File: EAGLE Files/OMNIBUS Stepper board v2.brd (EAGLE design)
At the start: 100.6 x 73.6 mm, 52 parts, among them IC1 REG1117, K7 691131710005, K8 691131710005, K9 691131710005, Q1 BTS134D, U2 L7805ACD2T-TR

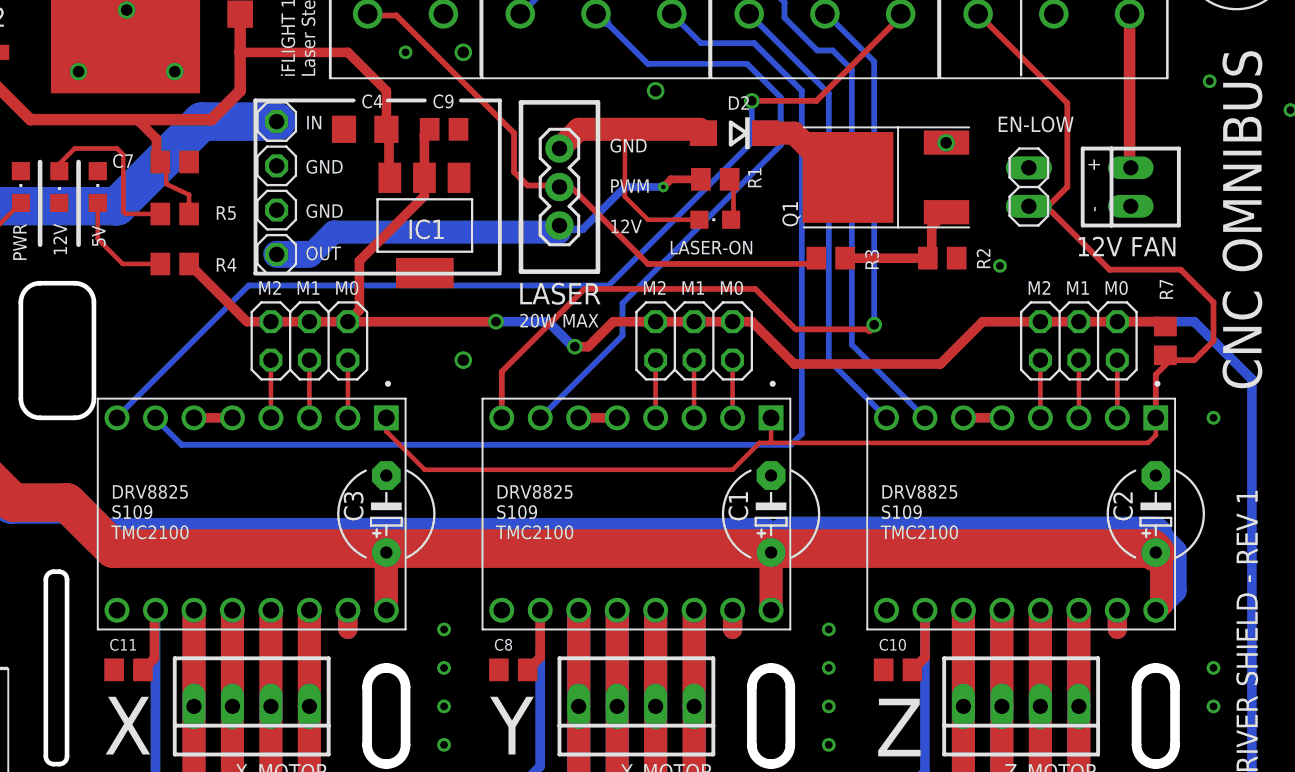
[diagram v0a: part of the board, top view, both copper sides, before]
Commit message: PCB Bugfixes and polishing
• DRV Shield had an routing error (laser indicator LED) also R3 had a wrong value
• New Footprint for the 0.33uF Caps
• Silkscreen polishing
• almost all LEDs are 0805 package now
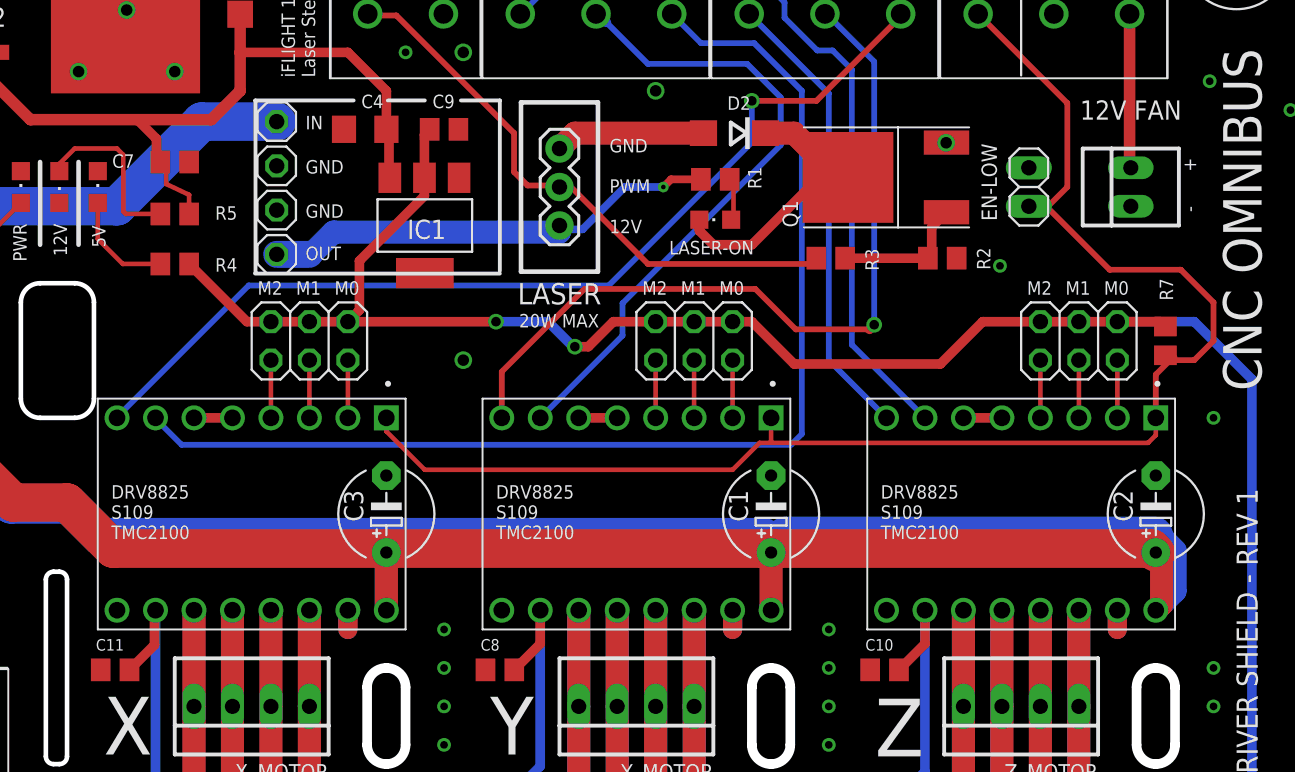
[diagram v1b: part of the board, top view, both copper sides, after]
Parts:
- R3: value 10k -> 470
- moved C11 0.89 mm to (18.9, 20.2)
- moved C8 0.89 mm to (44.3, 20.2)
- moved C10 0.89 mm to (69.7, 20.2)
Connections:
- net L_SW: now also D2.C, Q1.T; no longer D2.A, J1.3
- net N$4: now also D2.A, J1.3; no longer D2.C, Q1.T
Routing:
- net N$4: track 8.10 -> 9.93 mm
- net 5V: track 286.8 -> 287.9 mm
- net L_SW: track 20.1 -> 19.3 mm
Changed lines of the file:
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@@
 <drawing>
 <settings>
-<setting alwaysvectorfont="no"/>
+<setting alwaysvectorfont="yes"/>
 <setting verticaltext="up"/>
 </settings>
@@
 <text x="80.645" y="71.501" size="0.889" layer="25" font="vector" ratio="15" rot="SR180" align="bottom-center">GND</text>
 <text x="85.217" y="71.501" size="0.889" layer="25" font="vector" ratio="15" rot="SR180" align="bottom-center">12V-OUT</text>
-<text x="85.725" y="47.498" size="1.27" layer="25" font="vector" ratio="15" align="bottom-center">12V FAN</text>
+<text x="85.979" y="56.515" size="1.27" layer="25" font="vector" ratio="15" align="bottom-center">12V FAN</text>
 <text x="94.615" y="49.911" size="2.54" layer="25" font="vector" ratio="20" rot="SR90" align="bottom-center">CNC OMNIBUS</text>
 <text x="94.361" y="22.098" size="1.397" layer="25" font="vector" ratio="15" rot="SR90" align="bottom-center">DRIVER SHIELD - REV 1</text>
@@
 <wire x1="13.97" y1="53.721" x2="13.97" y2="48.26" width="0.3048" layer="25"/>
 <wire x1="16.51" y1="53.721" x2="16.51" y2="48.26" width="0.3048" layer="25"/>
-<text x="83.947" y="53.086" size="0.889" layer="25" font="vector" ratio="15" rot="R90">+</text>
+<text x="90.297" y="53.086" size="0.889" layer="25" font="vector" ratio="15" rot="R90">+</text>
 <text x="29.972" y="45.847" size="0.889" layer="25" font="vector" ratio="15" rot="R180">M2</text>
 <text x="32.512" y="45.847" size="0.889" layer="25" font="vector" ratio="15" rot="R180">M1</text>
@@
 TMC2100</text>
 <text x="-0.508" y="37.338" size="0.889" layer="25" font="vector" ratio="15" rot="SR270">MAX CURRENT: 10A</text>
-<text x="83.947" y="50.419" size="0.889" layer="25" font="vector" ratio="15" rot="R90">-</text>
+<text x="90.297" y="50.419" size="0.889" layer="25" font="vector" ratio="15" rot="R90">-</text>
 <text x="44.069" y="28.829" size="0.889" layer="25" font="vector" ratio="15">DRV8825
 S109
@@
 </element>
 <element name="EN-LOW" library="pinhead" library_urn="urn:adsk.eagle:library:325" package="1X02" package3d_urn="urn:adsk.eagle:package:22435/2" value="" x="79.248" y="52.07" smashed="yes" rot="R270">
-<attribute name="NAME" x="82.2452" y="56.7182" size="1.016" layer="25" font="vector" ratio="10" rot="R180"/>
+<attribute name="NAME" x="76.1238" y="54.9402" size="1.016" layer="25" font="vector" ratio="20" rot="R270"/>
 <attribute name="POPULARITY" value="98" x="79.248" y="52.07" size="1.778" layer="27" rot="R270" display="off"/>
 <attribute name="VALUE" x="76.073" y="54.61" size="1.27" layer="27" rot="R270"/>
@@
 <attribute name="VALUE" x="63.319" y="1.592" size="1.27" layer="27"/>
 </element>
-<element name="R3" library="rcl" library_urn="urn:adsk.eagle:library:334" package="R0805" package3d_urn="urn:adsk.eagle:package:23553/2" value="10k" x="66.167" y="47.371" smashed="yes" rot="R180">
+<element name="R3" library="rcl" library_urn="urn:adsk.eagle:library:334" package="R0805" package3d_urn="urn:adsk.eagle:package:23553/2" value="470" x="66.167" y="47.371" smashed="yes" rot="R180">
 <attribute name="NAME" x="68.453" y="48.006" size="0.889" layer="25" font="vector" ratio="10" rot="R270"/>
 <attribute name="POPULARITY" value="86" x="66.167" y="47.371" size="1.778" layer="27" rot="R180" display="off"/>
@@
 <attribute name="VALUE" x="28.321" y="44.45" size="1.27" layer="27"/>
 </element>
-<element name="C8" library="rcl" library_urn="urn:adsk.eagle:library:334" package="C0805" package3d_urn="urn:adsk.eagle:package:23617/2" value="100nf" x="45.212" y="20.193" smashed="yes">
-<attribute name="NAME" x="43.942" y="21.463" size="0.762" layer="25" font="vector" ratio="10"/>
-<attribute name="SPICEPREFIX" value="C" x="45.212" y="20.193" size="1.778" layer="27" display="off"/>
-<attribute name="VALUE" x="43.942" y="17.653" size="1.27" layer="27"/>
-</element>
-<element name="C10" library="rcl" library_urn="urn:adsk.eagle:library:334" package="C0805" package3d_urn="urn:adsk.eagle:package:23617/2" value="100nf" x="70.612" y="20.193" smashed="yes">
-<attribute name="NAME" x="69.342" y="21.463" size="0.762" layer="25" font="vector" ratio="10"/>
-<attribute name="SPICEPREFIX" value="C" x="70.612" y="20.193" size="1.778" layer="27" display="off"/>
-<attribute name="VALUE" x="69.342" y="17.653" size="1.27" layer="27"/>
-</element>
-<element name="C11" library="rcl" library_urn="urn:adsk.eagle:library:334" package="C0805" package3d_urn="urn:adsk.eagle:package:23617/2" value="100nf" x="19.812" y="20.193" smashed="yes">
-<attribute name="NAME" x="18.542" y="21.463" size="0.762" layer="25" font="vector" ratio="10"/>
-<attribute name="SPICEPREFIX" value="C" x="19.812" y="20.193" size="1.778" layer="27" display="off"/>
-<attribute name="VALUE" x="18.542" y="17.653" size="1.27" layer="27"/>
+<element name="C8" library="rcl" library_urn="urn:adsk.eagle:library:334" package="C0805" package3d_urn="urn:adsk.eagle:package:23617/2" value="100nf" x="44.323" y="20.193" smashed="yes">
+<attribute name="NAME" x="43.053" y="21.463" size="0.762" layer="25" font="vector" ratio="10"/>
+<attribute name="SPICEPREFIX" value="C" x="44.323" y="20.193" size="1.778" layer="27" display="off"/>
+<attribute name="VALUE" x="43.053" y="17.653" size="1.27" layer="27"/>
+</element>
+<element name="C10" library="rcl" library_urn="urn:adsk.eagle:library:334" package="C0805" package3d_urn="urn:adsk.eagle:package:23617/2" value="100nf" x="69.723" y="20.193" smashed="yes">
+<attribute name="NAME" x="68.453" y="21.463" size="0.762" layer="25" font="vector" ratio="10"/>
+<attribute name="SPICEPREFIX" value="C" x="69.723" y="20.193" size="1.778" layer="27" display="off"/>
+<attribute name="VALUE" x="68.453" y="17.653" size="1.27" layer="27"/>
+</element>
+<element name="C11" library="rcl" library_urn="urn:adsk.eagle:library:334" package="C0805" package3d_urn="urn:adsk.eagle:package:23617/2" value="100nf" x="18.923" y="20.193" smashed="yes">
+<attribute name="NAME" x="17.653" y="21.463" size="0.762" layer="25" font="vector" ratio="10"/>
+<attribute name="SPICEPREFIX" value="C" x="18.923" y="20.193" size="1.778" layer="27" display="off"/>
+<attribute name="VALUE" x="17.653" y="17.653" size="1.27" layer="27"/>
 </element>
 </elements>
@@
 <contactref element="C11" pad="2"/>
 <contactref element="C8" pad="2"/>
-<wire x1="21.524" y1="24.064" x2="21.524" y2="20.955" width="0.635" layer="1"/>
-<wire x1="20.762" y1="20.193" x2="21.524" y2="20.955" width="0.635" layer="1"/>
+<wire x1="21.524" y1="24.064" x2="21.524" y2="21.844" width="0.635" layer="1"/>
+<wire x1="19.873" y1="20.193" x2="21.524" y2="21.844" width="0.635" layer="1"/>
 <wire x1="21.524" y1="24.064" x2="21.59" y2="24.13" width="0.635" layer="1"/>
-<wire x1="46.162" y1="20.193" x2="46.99" y2="21.021" width="0.635" layer="1"/>
-<wire x1="46.99" y1="21.021" x2="46.99" y2="24.13" width="0.635" layer="1"/>
-<wire x1="71.562" y1="20.193" x2="72.39" y2="21.021" width="0.635" layer="1"/>
-<wire x1="72.39" y1="21.021" x2="72.39" y2="24.13" width="0.635" layer="1"/>
+<wire x1="45.273" y1="20.193" x2="46.99" y2="21.91" width="0.635" layer="1"/>
+<wire x1="46.99" y1="21.91" x2="46.99" y2="24.13" width="0.635" layer="1"/>
+<wire x1="70.673" y1="20.193" x2="72.39" y2="21.91" width="0.635" layer="1"/>
+<wire x1="72.39" y1="21.91" x2="72.39" y2="24.13" width="0.635" layer="1"/>
 </signal>
 <signal name="X_DIR" class="1">
@@
 </signal>
 <signal name="L_SW" class="1">
-<contactref element="D2" pad="A"/>
 <contactref element="LASER-ON" pad="C"/>
-<wire x1="52.578" y1="55.88" x2="57.513" y2="55.88" width="1.524" layer="1"/>
-<wire x1="57.513" y1="55.88" x2="57.767" y2="55.626" width="1.524" layer="1"/>
-<wire x1="57.497" y1="49.911" x2="54.102" y2="49.911" width="0.3048" layer="1"/>
-<wire x1="54.102" y1="49.911" x2="52.578" y2="51.435" width="0.3048" layer="1"/>
-<wire x1="52.578" y1="51.435" x2="52.578" y2="55.88" width="0.3048" layer="1"/>
-<contactref element="J1" pad="3"/>
-<wire x1="52.578" y1="55.88" x2="49.53" y2="55.88" width="1.524" layer="1"/>
-<wire x1="49.53" y1="55.88" x2="48.26" y2="54.61" width="1.524" layer="1"/>
+<contactref element="D2" pad="C"/>
+<contactref element="Q1" pad="T"/>
+<wire x1="61.867" y1="55.626" x2="63.754" y2="55.626" width="1.524" layer="1"/>
+<wire x1="63.754" y1="55.626" x2="66.04" y2="53.34" width="1.524" layer="1"/>
+<wire x1="66.04" y1="51.943" x2="66.04" y2="53.34" width="1.524" layer="1"/>
+<wire x1="67.31" y1="52.705" x2="66.548" y2="51.943" width="0.635" layer="1"/>
+<wire x1="66.548" y1="51.943" x2="66.04" y2="51.943" width="0.635" layer="1"/>
+<wire x1="57.497" y1="49.911" x2="57.497" y2="49.183" width="0.635" layer="1"/>
+<wire x1="57.497" y1="49.183" x2="58.42" y2="48.26" width="0.635" layer="1"/>
+<wire x1="58.42" y1="48.26" x2="60.96" y2="48.26" width="0.635" layer="1"/>
+<wire x1="64.643" y1="51.943" x2="66.04" y2="51.943" width="0.635" layer="1"/>
+<wire x1="60.96" y1="48.26" x2="64.643" y2="51.943" width="0.635" layer="1"/>
 </signal>
 <signal name="5VPWM" class="1">
@@
 <contactref element="JP1" pad="1"/>
 </signal>
-<signal name="N$4" class="1">
-<contactref element="D2" pad="C"/>
-<wire x1="61.867" y1="55.626" x2="63.754" y2="55.626" width="1.524" layer="1"/>
-<wire x1="63.754" y1="55.626" x2="66.04" y2="53.34" width="1.524" layer="1"/>
-<wire x1="66.04" y1="51.943" x2="66.04" y2="53.34" width="1.524" layer="1"/>
-<contactref element="Q1" pad="T"/>
-<wire x1="67.31" y1="52.705" x2="66.548" y2="51.943" width="0.635" layer="1"/>
-<wire x1="66.548" y1="51.943" x2="66.04" y2="51.943" width="0.635" layer="1"/>
-</signal>
 <signal name="N$2">
 <contactref element="R4" pad="2"/>
@@
 <wire x1="26.67" y1="36.83" x2="24.13" y2="36.83" width="0.635" layer="1"/>
 </signal>
+<signal name="N$4" class="1">
+<contactref element="D2" pad="A"/>
+<contactref element="J1" pad="3"/>
+<wire x1="48.26" y1="54.61" x2="49.276" y2="55.626" width="1.524" layer="1"/>
+<wire x1="49.276" y1="55.626" x2="57.767" y2="55.626" width="1.524" layer="1"/>
+</signal>
 </signals>

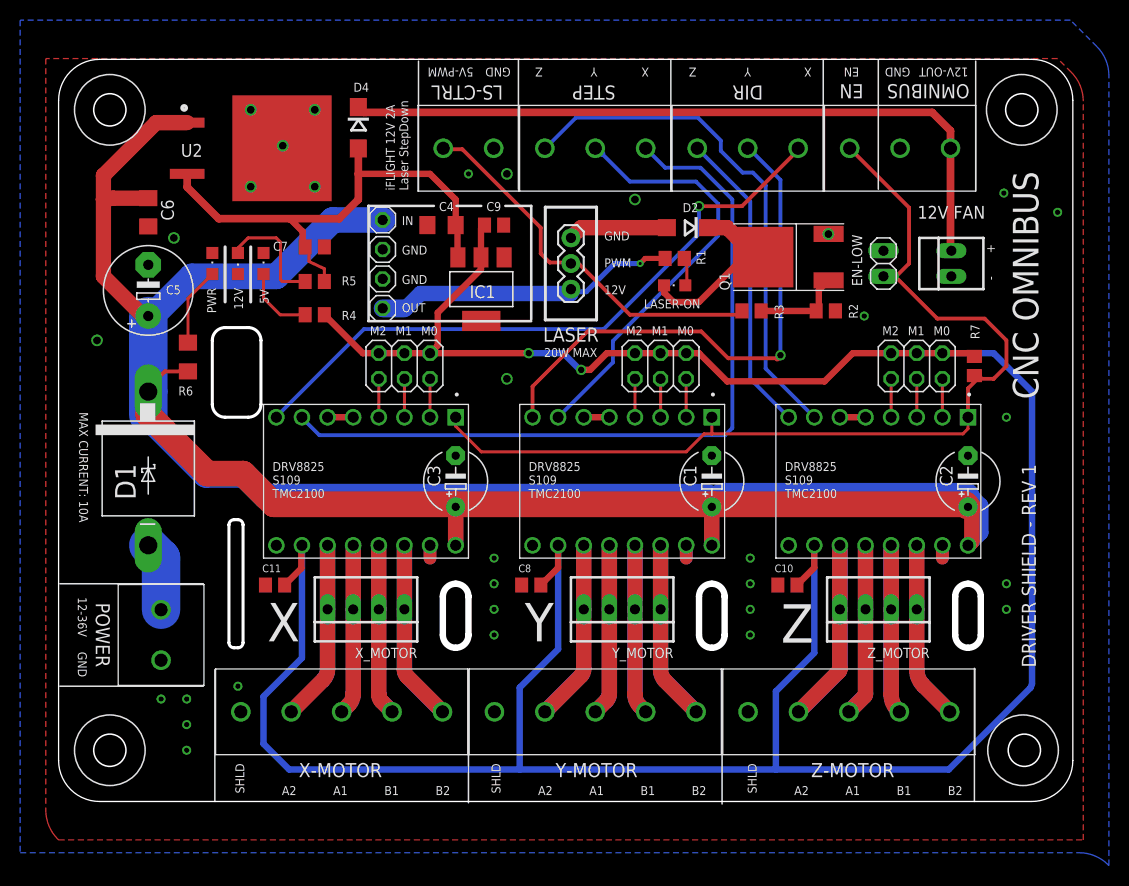
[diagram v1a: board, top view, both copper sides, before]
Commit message: Changed voltage regulators
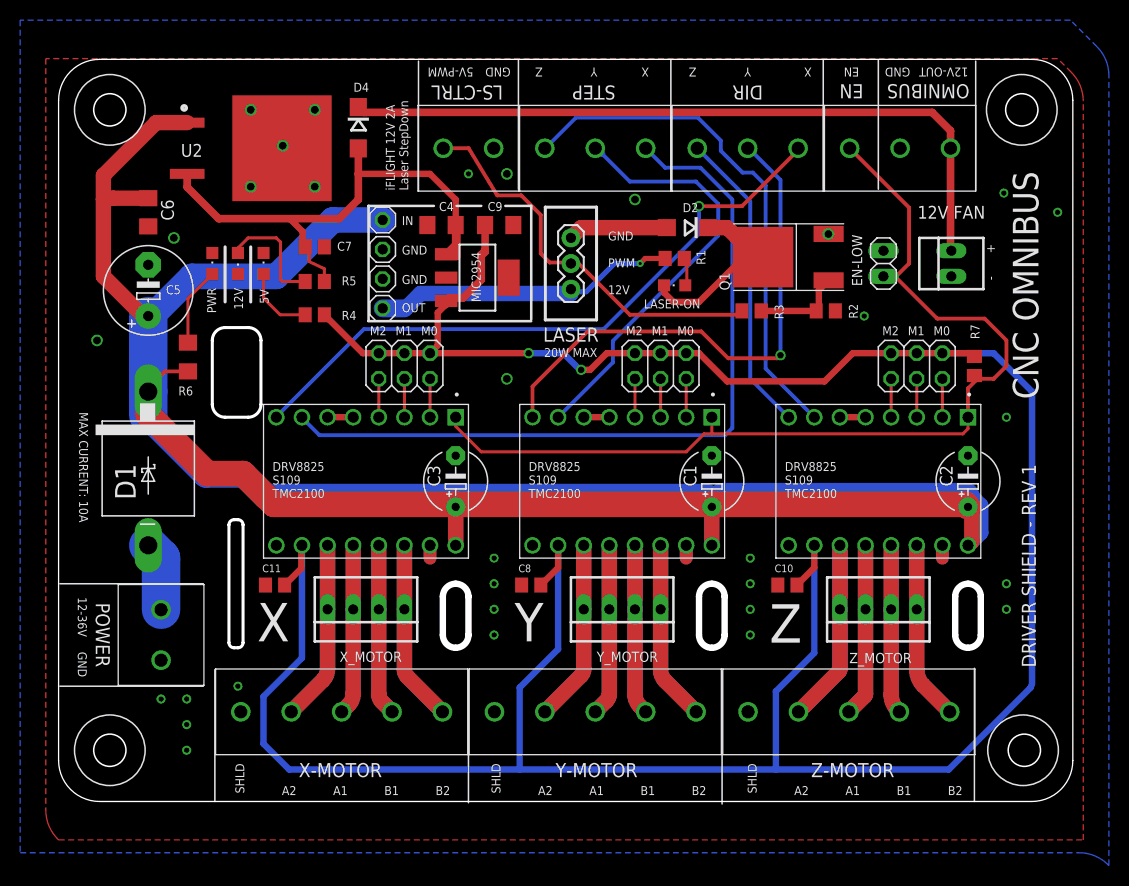
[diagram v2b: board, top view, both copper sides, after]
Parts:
- removed IC1: REG1117, burr-brown:SOT223
- added MIC2954: MIC2954, MIC2954:SOT223
- C9: device rcl:C0805 -> rcl:C1206
- moved C9 0.51 mm to (41.1, 55.9)
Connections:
- net N$4 renamed GND_SW
- net 12V_BD: now also MIC2954.1; no longer IC1.3
- net 5V: now also MIC2954.3; no longer IC1.2
- net GND: now also MIC2954.2, MIC2954.4; no longer IC1.1
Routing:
- net 12V_BD: track 50.0 -> 53.2 mm
- net 5VPWM: track 38.2 -> 39.6 mm
- net 5V: track 287.9 -> 289.1 mm

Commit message: clean up
also added BOM
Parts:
- 12V, 5V, PWR: value (none) -> green
- renumbered RAW1 to PWM
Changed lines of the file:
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@@
 <drawing>
 <settings>
-<setting alwaysvectorfont="yes"/>
+<setting alwaysvectorfont="no"/>
 <setting verticaltext="up"/>
 </settings>
@@
 <attribute name="VALUE" x="9.3726" y="46.8884" size="1.27" layer="27" ratio="10" rot="R90"/>
 </element>
-<element name="RAW1" library="Wurth_Terminal_Blocks_Connectors_rev15d" package="691131710002" value="691131710002" x="38.1" y="63.5" smashed="yes" rot="R180">
+<element name="PWM" library="Wurth_Terminal_Blocks_Connectors_rev15d" package="691131710002" value="691131710002" x="38.1" y="63.5" smashed="yes" rot="R180">
 <attribute name="VALUE" x="43.1" y="69.528" size="1.27" layer="27" rot="R180"/>
 </element>
@@
 <attribute name="VALUE" x="23.495" y="49.53" size="1.27" layer="27" rot="R180"/>
 </element>
-<element name="5V" library="led" library_urn="urn:adsk.eagle:library:259" package="CHIPLED_0805" package3d_urn="urn:adsk.eagle:package:15821/2" value="" x="17.78" y="52.07" smashed="yes">
+<element name="5V" library="led" library_urn="urn:adsk.eagle:library:259" package="CHIPLED_0805" package3d_urn="urn:adsk.eagle:package:15821/2" value="green" x="17.78" y="52.07" smashed="yes">
 <attribute name="NAME" x="17.399" y="49.53" size="0.889" layer="25" font="vector" ratio="10" rot="R270"/>
 <attribute name="VALUE" x="20.32" y="50.8" size="1.27" layer="27" rot="R90"/>
@@
 <attribute name="VALUE" x="23.495" y="52.832" size="1.27" layer="27" rot="R180"/>
 </element>
-<element name="12V" library="led" library_urn="urn:adsk.eagle:library:259" package="CHIPLED_0805" package3d_urn="urn:adsk.eagle:package:15821/2" value="" x="15.24" y="52.07" smashed="yes" rot="R180">
+<element name="12V" library="led" library_urn="urn:adsk.eagle:library:259" package="CHIPLED_0805" package3d_urn="urn:adsk.eagle:package:15821/2" value="green" x="15.24" y="52.07" smashed="yes" rot="R180">
 <attribute name="NAME" x="14.859" y="49.657" size="0.889" layer="25" font="vector" ratio="10" rot="R270"/>
 <attribute name="VALUE" x="12.7" y="53.34" size="1.27" layer="27" rot="R270"/>
@@
 <attribute name="VALUE" x="12.827" y="42.164" size="1.27" layer="27" rot="R90"/>
 </element>
-<element name="PWR" library="led" library_urn="urn:adsk.eagle:library:259" package="CHIPLED_0805" package3d_urn="urn:adsk.eagle:package:15821/2" value="" x="12.7" y="52.07" smashed="yes">
+<element name="PWR" library="led" library_urn="urn:adsk.eagle:library:259" package="CHIPLED_0805" package3d_urn="urn:adsk.eagle:package:15821/2" value="green" x="12.7" y="52.07" smashed="yes">
 <attribute name="NAME" x="12.192" y="49.657" size="0.889" layer="25" font="vector" ratio="10" rot="R270"/>
 <attribute name="VALUE" x="15.24" y="50.8" size="1.27" layer="27" rot="R90"/>
@@
 <contactref element="K7" pad="1"/>
 <contactref element="R2" pad="2"/>
-<contactref element="RAW1" pad="1"/>
+<contactref element="PWM" pad="1"/>
 <contactref element="C5" pad="-"/>
 <contactref element="12V" pad="C"/>
@@
 <signal name="5VPWM" class="1">
 <contactref element="R3" pad="2"/>
-<contactref element="RAW1" pad="2"/>
+<contactref element="PWM" pad="2"/>
 <wire x1="35.6" y1="63.5" x2="35.56" y2="63.5" width="0.3048" layer="16"/>
 <wire x1="64.836" y1="46.99" x2="65.217" y2="47.371" width="0.381" layer="1"/>
